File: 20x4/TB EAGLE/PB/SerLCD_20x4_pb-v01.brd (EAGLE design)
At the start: 73.7 x 139.7 mm, 21 parts, among them J1 AVR_PROG, J3 SER_LCD16X2, U1 5V Flying Jalapeno, U2 74LVC4066_MUX_1:1_X4

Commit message: finshed up 20x4, RFR
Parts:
- added U$1, U$2: (no value), SparkFun:STAND-OFF-TIGHT
- J3: value SER_LCD16X2 -> SER_LCD20X4; device SerLCD_dimensions:SER_LCD_16X2 -> SerLCD_dimensions:SER_LCD_20X4
- moved U$3 37.8 mm to (97.8, 139.7)
- moved U1 29.0 mm to (50.8, 165.1)
- moved J3 28.1 mm to (85.1, 31.8)
- moved U$8 27.9 mm to (97.8, 22.9)
- moved JP3 25.4 mm to (20.3, 149.9)
- moved J1 25.4 mm to (5.08, 148.6)
- moved JP2 25.4 mm to (10.2, 146.1)
- moved U2 25.4 mm to (15.2, 146.1)
- moved JP1 25.4 mm to (10.2, 143.5)
- moved JP4 25.4 mm to (20.3, 147.3)
- moved U$6 25.4 mm to (0.00, 124.5)
- moved LED3 17.8 mm to (86.4, 11.4)
- moved LED4 17.8 mm to (86.4, 5.08)
- moved 2 17.8 mm to (69.8, 10.2)
- moved LED1 10.2 mm to (40.6, 11.4)
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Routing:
- net RST: track 34.0 -> 130.4 mm, vias 0 -> 1
- net MISO: track 129.4 -> 203.9 mm, vias 3 -> 1
- net MOSI: track 149.6 -> 202.9 mm, vias 2 -> 1
- net SCL: track 95.4 -> 139.1 mm, vias 1 -> 0
- net SCK: track 141.6 -> 179.0 mm, vias 3 -> 2
- net DTR_FJ: track 107.0 -> 143.8 mm, vias 1 -> 0
- net TX1_FJ: track 130.0 -> 166.5 mm
- net CS: track 115.1 -> 150.5 mm, vias 0 -> 1
- net N$2: track 131.4 -> 163.9 mm
- net N$6: track 186.6 -> 219.1 mm, vias 1 -> 0
- net SDA: track 91.1 -> 123.3 mm
- net N$1: track 129.6 -> 156.5 mm
- net N$5: track 180.7 -> 206.7 mm
- net N$7: track 105.7 -> 130.5 mm, vias 0 -> 1
- net 3.3_VCC: track 105.9 -> 129.0 mm
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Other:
- board size 73.7 x 139.7 mm -> 101.6 x 165.1 mm
- board text added: "#580"
- board text added: "Serial LCD 20x4"
- board text removed: "#579"
- board text removed: "Serial LCD 16x4"

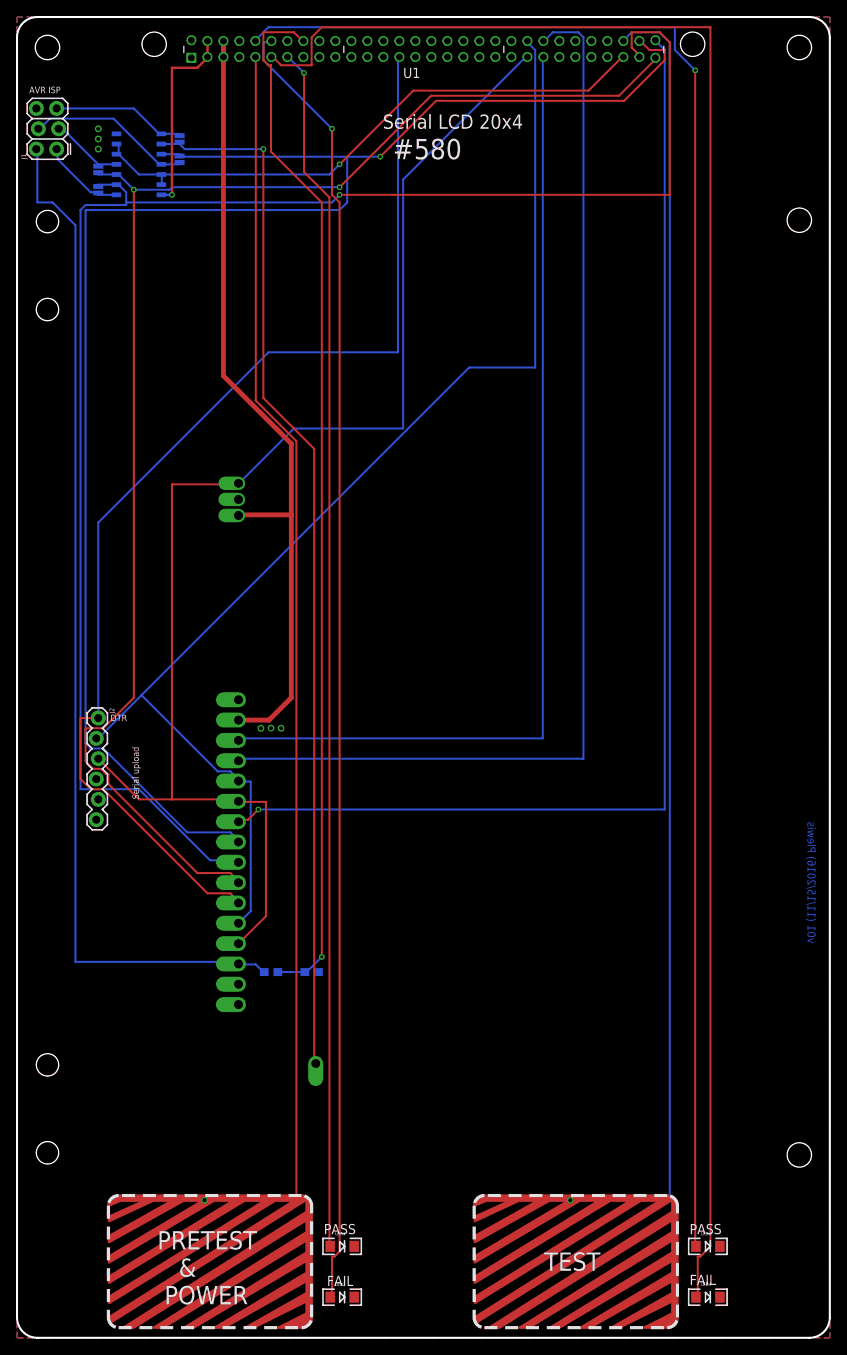
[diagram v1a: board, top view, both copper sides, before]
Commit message: added preTest to 3.3V output on 20x4
ready to order both designs... gonna throw on a QC panel asap
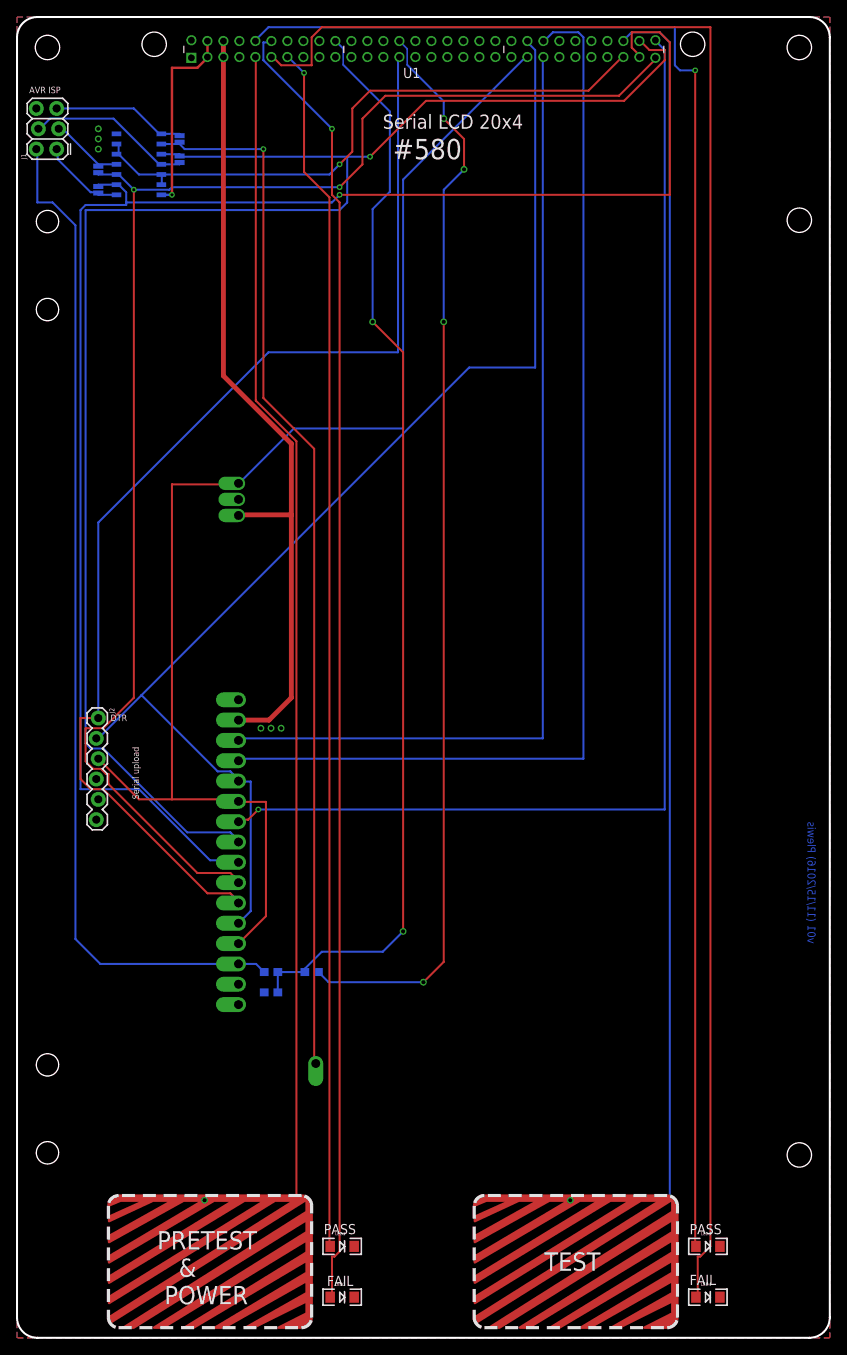
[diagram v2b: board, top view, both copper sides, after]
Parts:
- removed R1, R2: 10k, SparkFun-Resistors:0603
- added R5, R6: 10K, SparkFun-Resistors:0603-RES
- added R7: 100k, SparkFun-Resistors:0603-RES
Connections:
- removed net N$7: R1.1, R2.2, U1.38
- new net PT_CTRL: R5.1, U1.44
- new net PT_READ_3.3V: R5.2, R6.1, R7.2, U1.40
- net 3.3_VCC: now also R6.2; no longer R1.2
- net GND: now also R7.1; no longer R2.1
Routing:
- net PT_READ_3.3V: track 0.00 -> 137.2 mm, vias 0 -> 2
- net PT_CTRL: track 0.00 -> 136.7 mm, vias 0 -> 4
- net N$7: track 130.5 -> 0.00 mm, vias 1 -> 0
- net SCK: track 179.0 -> 182.4 mm
- net PGM_SWITCH_EN: track 73.3 -> 76.5 mm
- net 3.3_VCC: track 129.0 -> 127.3 mm
- net N$5: track 206.7 -> 207.9 mm
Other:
- board text added: "100K"
